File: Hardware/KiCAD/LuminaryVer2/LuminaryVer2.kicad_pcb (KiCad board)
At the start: 4 copper layers, 25.7 x 50 mm, 72 parts, among them J1 JTAG, J10 ExtBattPwr, J12 USB_B_Micro, J13 CN1, J14 CN2, J2 GPIOInput, Q1 2N3904, SW1 SW_Push, SW2 SW_BATT_DISCONNECT, U1 74HC14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

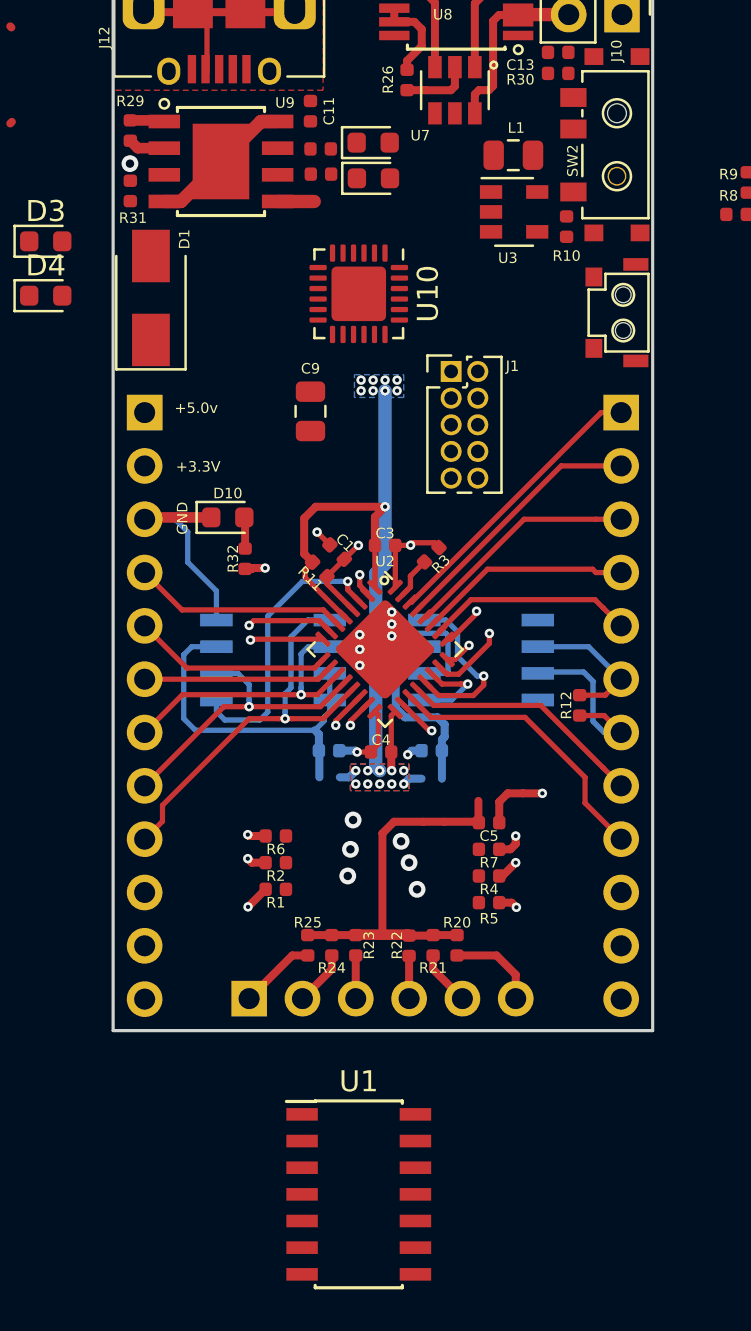
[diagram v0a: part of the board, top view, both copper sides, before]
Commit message: Add silk screen overlay to pins. Redo GPIO input to use LCSC basic part.
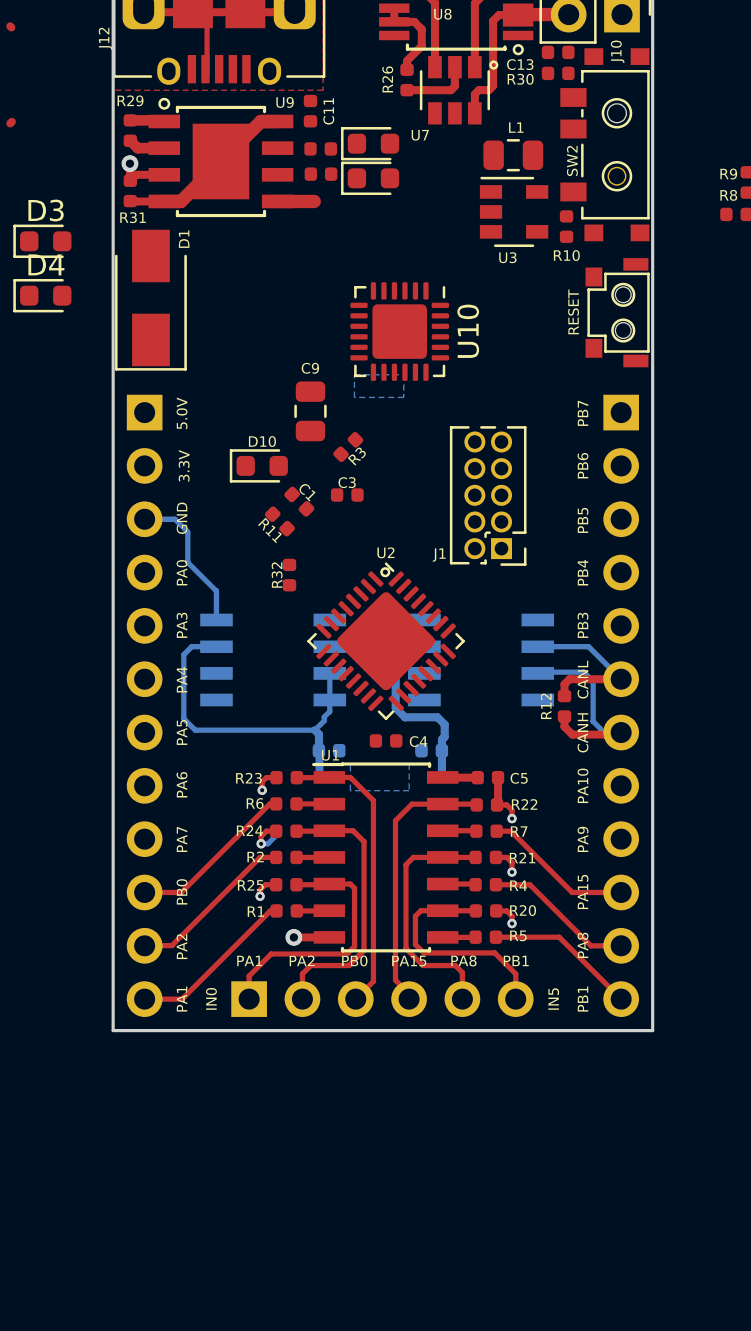
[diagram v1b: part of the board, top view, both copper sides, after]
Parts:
- moved U1 16.1 mm to (223.9, 91.8)
- moved J1 8.77 mm to (229.4, 77.0), turned to 180 degrees
- moved R23 8.64 mm to (219.2, 88.0), turned to 0 degrees
- moved R22 7.66 mm to (228.7, 89.2), turned to 180 degrees
- moved R3 6.49 mm to (222.1, 72.2)
- moved R24 5.85 mm to (219.2, 90.5), turned to 0 degrees
- moved R21 4.88 mm to (228.7, 91.8), turned to 180 degrees
- moved R25 3.06 mm to (219.2, 93.0), turned to 0 degrees
- moved C1 3.00 mm to (219.8, 74.8)
- moved C3 3.00 mm to (222.1, 74.5)
- moved R11 2.97 mm to (218.8, 75.7)
- moved D10 2.95 mm to (218.0, 73.1)
- moved U10 2.65 mm to (224.6, 66.7)
- moved R32 2.25 mm to (219.3, 78.3)
- moved C5 2.14 mm to (228.8, 88.0)
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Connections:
- R20 pad 1: +3V3 -> GND
- R21 pad 1: +3V3 -> GND
- R22 pad 1: +3V3 -> GND
- R23 pad 1: +3V3 -> GND
- R24 pad 1: +3V3 -> GND
- R25 pad 1: +3V3 -> GND
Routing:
- net +3V3: track 80.8 -> 27.6 mm, vias 19 -> 0
- net /Output Connectors/SPI_1_MOSI: track 19.5 -> 0.00 mm, vias 1 -> 0
- net /Output Connectors/SPI_1_MISO: track 14.4 -> 0.00 mm, vias 1 -> 0
- net /Output Connectors/SPI_1_SCK: track 13.8 -> 0.00 mm, vias 1 -> 0
- net /Output Connectors/I2C_1_SDA: track 13.8 -> 0.00 mm
- net FlashCS: track 13.6 -> 0.00 mm, vias 1 -> 0
- net /Output Connectors/RS232_1_TX: track 13.6 -> 0.00 mm
- net /Output Connectors/I2C_1_SCL: track 12.5 -> 0.00 mm
- net /Processor/GPIO_0: track 20.2 -> 8.02 mm, vias 2 -> 0
- net /Output Connectors/RS232_1_RX: track 11.6 -> 0.00 mm
- net /Output Connectors/SPI_2_MOSI: track 11.3 -> 0.00 mm
- net /Processor/ADC_0: track 10.2 -> 0.00 mm
- net /Output Connectors/SPI_2_MISO: track 10.1 -> 0.00 mm
- net /Output Connectors/SPI_2_SCK: track 9.81 -> 0.00 mm
- net /Processor/ADC_1: track 9.49 -> 0.00 mm
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- removed copper zone on F.Cu, net +3V3
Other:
- board text added: "3.3V"
- board text added: "5.0V"
- board text added: "CANH"
- board text added: "CANL"
- board text added: "IN0"
- board text added: "IN5"
- board text added: "PA0"
- board text added: "PA1"
- board text added: "PA10"
- board text added: "PA15"
- board text added: "PA2"
- board text added: "PA3"
- board text added: "PA4"
- board text added: "PA5"
- board text added: "PA6"
- board text added: "PA7"
- board text added: "PA8"
- board text added: "PA9"
- board text added: "PB0"
- board text added: "PB1"
- board text added: "PB3"
- board text added: "PB4"
- board text added: "PB5"
- board text added: "PB6"
- board text added: "PB7"
- board text added: "RESET"
- board text removed: "+3.3V"
- board text removed: "+5.0v"

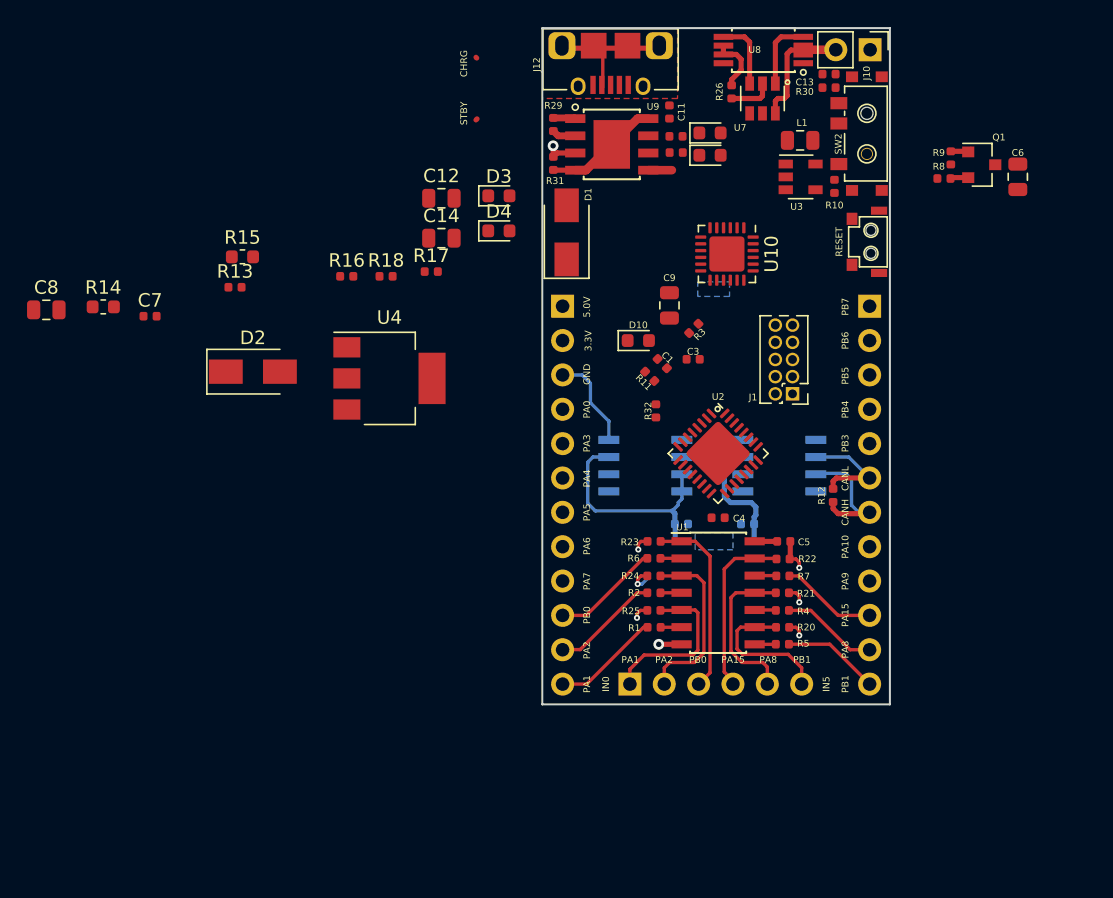
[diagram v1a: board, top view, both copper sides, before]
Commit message: Laid out the power supply updates.
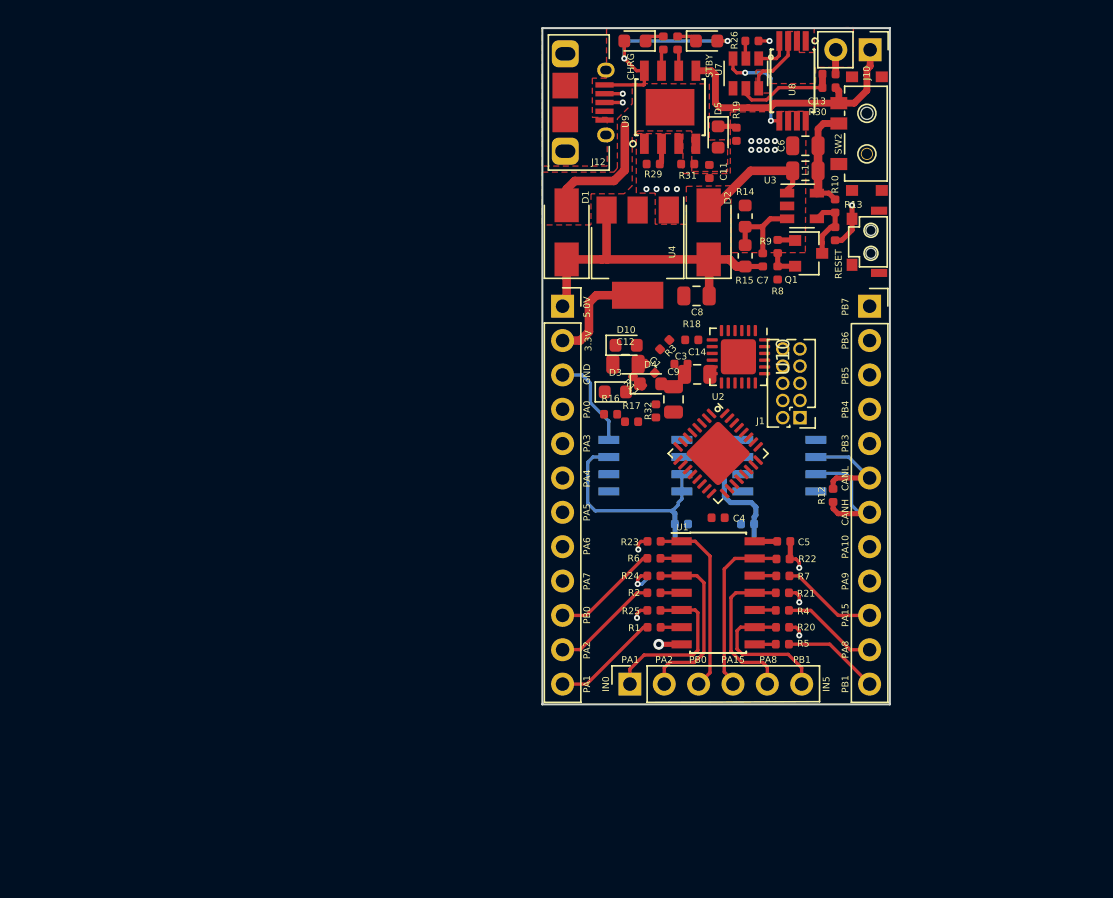
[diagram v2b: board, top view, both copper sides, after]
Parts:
- added D5: BLED, Diode_SMD:D_0603_1608Metric, F.Cu at (223.9, 58.0)
- added R19: 1k, Resistor_SMD:R_0402_1005Metric, F.Cu at (225.2, 57.9)
- moved C8 48.1 mm to (222.3, 69.8)
- moved R14 47.9 mm to (225.9, 63.9), turned to 270 degrees
- moved C7 45.5 mm to (227.2, 67.1), turned to 90 degrees
- moved R13 44.5 mm to (232.6, 65.2), turned to 90 degrees
- moved R15 37.2 mm to (225.9, 66.8), turned to 90 degrees
- moved D2 35.2 mm to (223.2, 65.1), turned to 90 degrees
- moved R18 23.1 mm to (221.9, 73.0)
- moved R16 22.0 mm to (215.9, 78.5)
- moved C14 21.4 mm to (222.3, 75.6)
- moved U4 20.6 mm to (217.9, 66.6), turned to 270 degrees
- moved R17 18.5 mm to (217.5, 79.1)
- moved C12 18.3 mm to (217.1, 74.8)
- moved D3 16.9 mm to (216.3, 76.9)
- moved D4 15.9 mm to (218.9, 76.3)
- moved C6 15.9 mm to (230.3, 58.7), turned to 0 degrees
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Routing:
- net +5V: track 0.00 -> 24.7 mm
- net /Power Supply/Ext_In+: track 8.60 -> 27.0 mm, vias 0 -> 2
- net /Input Connectors/Batt_V+: track 2.00 -> 20.2 mm
- net GND: track 38.5 -> 24.0 mm, vias 8 -> 21
- net Net-(D2-Pad2): track 0.00 -> 9.09 mm
- net +3V3: track 27.6 -> 35.7 mm
- net Net-(C6-Pad2): track 0.00 -> 8.03 mm
- net Net-(C13-Pad1): track 0.00 -> 7.65 mm
- net Net-(C7-Pad2): track 0.00 -> 6.71 mm
- net Net-(Q1-Pad3): track 0.00 -> 5.15 mm
- net /Input Connectors/Batt_V-: track 9.42 -> 6.62 mm
- net Net-(U7-Pad1): track 5.27 -> 2.69 mm
- net Net-(U7-Pad3): track 5.17 -> 7.63 mm, vias 0 -> 2
- net Net-(R26-Pad1): track 3.27 -> 1.31 mm
- net Net-(R27-Pad1): track 0.00 -> 1.62 mm
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- added copper zone on F.Cu, net /Input Connectors/Batt_V-
- added copper zone on F.Cu, net /Power Supply/Ext_In+
- removed copper zone on B.Cu, net +3V3
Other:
- board text removed: "Luminary Ver 1.0"

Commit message: Routed most of the signal layer.
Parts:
- moved D3 33.4 mm to (249.6, 73.8)
- moved R17 32.5 mm to (248.3, 68.8)
- moved C12 31.7 mm to (248.4, 79.3)
- moved D4 31.3 mm to (249.9, 71.8)
- moved R16 31.3 mm to (246.9, 73.9)
- moved R18 25.4 mm to (247.2, 75.7)
- moved C14 21.8 mm to (244.2, 76.5)
- moved U10 18.3 mm to (243.6, 71.8)
- moved R11 15.4 mm to (232.4, 70.8), turned to 270 degrees
- moved C1 13.2 mm to (231.3, 70.8), turned to 90 degrees
- moved C9 7.77 mm to (221.9, 69.8), turned to 0 degrees
- moved R3 7.15 mm to (225.3, 78.2), turned to 90 degrees
- moved D10 5.18 mm to (216.5, 78.6)
- moved C3 4.12 mm to (223.7, 78.0)
- moved C8 3.19 mm to (225.5, 69.8)
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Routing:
- net +3V3: track 35.7 -> 84.1 mm, vias 0 -> 12
- net /Output Connectors/SPI_1_MOSI: track 0.00 -> 32.1 mm
- net /Output Connectors/SPI_1_MISO: track 0.00 -> 20.6 mm
- net /Output Connectors/I2C_1_SDA: track 0.00 -> 18.3 mm
- net GND: track 24.0 -> 41.3 mm, vias 21 -> 25
- net /Processor/GPIO_5: track 7.19 -> 24.5 mm, vias 0 -> 2
- net /Processor/GPIO_0: track 8.02 -> 25.2 mm, vias 0 -> 2
- net /Output Connectors/I2C_1_SCL: track 0.00 -> 15.3 mm
- net /Output Connectors/SPI_1_SCK: track 0.00 -> 14.4 mm, vias 0 -> 1
- net /Output Connectors/RS232_1_TX: track 0.00 -> 14.1 mm
- net /Output Connectors/SPI_2_MOSI: track 0.00 -> 12.9 mm
- net /Processor/GPIO_1: track 8.01 -> 20.8 mm, vias 0 -> 2
- net /Output Connectors/RS232_1_RX: track 0.00 -> 12.8 mm
- net /Processor/GPIO_3: track 7.14 -> 19.7 mm, vias 0 -> 2
- net /Processor/GPIO_4: track 7.17 -> 19.3 mm, vias 0 -> 2
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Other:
- board text added: "5.5V"
- board text added: "CAN Bus Transciever"
- board text added: "JTAG"
- board text added: "On Battery: 45mA On USB: 500mA"
- board text added: "SPI Flash Memory"
- board text added: "Single Cell Li-Ion Integrated Charger"
- board text added: "V+"
- board text added: "V-"

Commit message: Version two nets fully routed.
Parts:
- added R33: 1k, Resistor_SMD:R_0402_1005Metric, F.Cu at (219.6, 77.0)
- added R34: 1k, Resistor_SMD:R_0402_1005Metric, F.Cu at (219.6, 76.0)
- moved D4 33.7 mm to (216.3, 74.2), turned to 180 degrees
- moved D3 33.3 mm to (216.3, 72.0), turned to 180 degrees
- moved R17 29.7 mm to (218.9, 72.7), turned to 180 degrees
- moved R16 28.1 mm to (218.8, 71.5), turned to 180 degrees
- moved R18 24.3 mm to (223.3, 71.1), turned to 180 degrees
- moved C12 21.7 mm to (228.8, 69.8), turned to 180 degrees
- moved U10 20.3 mm to (223.3, 74.2), turned to 180 degrees
- moved C14 17.0 mm to (227.4, 73.8), turned to 270 degrees
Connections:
- U10 pad 20: /Output Connectors/RS232_1_TX -> Net-(R34-Pad1)
- U10 pad 21: /Output Connectors/RS232_1_RX -> Net-(R33-Pad1)
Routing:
- net /Output Connectors/RS232_1_RX: track 12.8 -> 58.9 mm, vias 0 -> 1
- net /Output Connectors/RS232_1_TX: track 14.1 -> 59.8 mm, vias 0 -> 1
- net /Input Connectors/D-: track 1.35 -> 30.1 mm, vias 1 -> 2
- net /Input Connectors/D+: track 1.35 -> 30.0 mm, vias 1 -> 2
- net /Power Supply/Ext_In+: track 27.0 -> 47.6 mm, vias 2 -> 14
- net /Input Connectors/nRESET: track 8.06 -> 23.8 mm, vias 0 -> 1
- net Net-(C14-Pad1): track 0.00 -> 11.2 mm, vias 0 -> 2
- net GND: track 41.3 -> 52.4 mm, vias 25 -> 35
- net Net-(R33-Pad1): track 0.00 -> 4.15 mm
- net Net-(R34-Pad1): track 0.00 -> 3.85 mm
- net Net-(R16-Pad1): track 0.00 -> 2.90 mm
- net Net-(D4-Pad1): track 0.00 -> 2.60 mm
- net Net-(R17-Pad1): track 0.00 -> 2.36 mm
- net Net-(D3-Pad1): track 0.00 -> 1.44 mm
- net Net-(R18-Pad1): track 0.00 -> 1.25 mm
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- added copper zone on B.Cu, net +3V3
- added copper zone on B.Cu, net /Power Supply/Ext_In+
